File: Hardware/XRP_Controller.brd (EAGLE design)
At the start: 63.5 x 54 mm, 219 parts, among them J1 POWER_JACKPOWER_JACK_SLOT, J12 Vertical Qwiic Connector, J13 Vertical Qwiic Connector, J14 Vertical Qwiic Connector, J3 JST_6_PIN_VERTICAL, J4 JST_6_PIN_VERTICAL, J5 JST_6_PIN_VERTICAL, J6 JST_6_PIN_VERTICAL, J9 Vertical Qwiic Connector, Q3 20V/4.2A/52mΩ/1.4W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

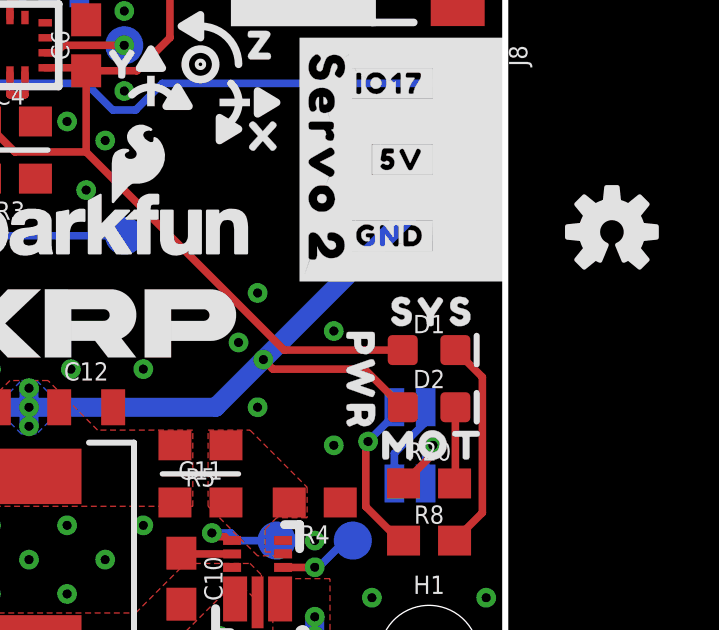
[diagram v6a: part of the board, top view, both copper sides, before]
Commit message: Put OSHW logo back onto board
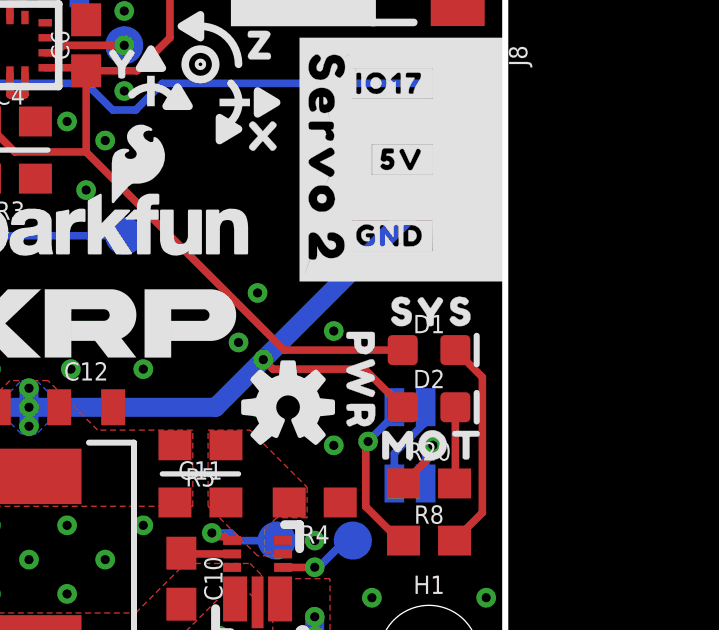
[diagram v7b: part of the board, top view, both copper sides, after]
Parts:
- moved LOGO1 12.3 mm to (56.3, 10.8)
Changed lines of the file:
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@@
 <element name="FD3" library="SparkFun-Aesthetics" package="FIDUCIAL-1X2" value="FIDUCIAL1X2" x="2.54" y="5.08" smashed="yes"/>
 <element name="FD4" library="SparkFun-Aesthetics" package="FIDUCIAL-1X2" value="FIDUCIAL1X2" x="2.54" y="5.08" smashed="yes" rot="MR0"/>
-<element name="LOGO1" library="SparkFun-Aesthetics" package="OSHW-LOGO-S" value="OSHW-LOGOS" x="67.056" y="16.637" smashed="yes"/>
+<element name="LOGO1" library="SparkFun-Aesthetics" package="OSHW-LOGO-S" value="OSHW-LOGOS" x="56.261" y="10.795" smashed="yes"/>
 <element name="LOGO3" library="SparkFun-Aesthetics" package="SFE_LOGO_NAME_FLAME_.3" value="SFE_LOGO_NAME_FLAME.3_INCH" x="37.465" y="41.91" smashed="yes" rot="MR0"/>
 <element name="H1" library="SparkFun-Hardware" package="STAND-OFF" value="STAND-OFF" x="60.96" y="2.54" smashed="yes">

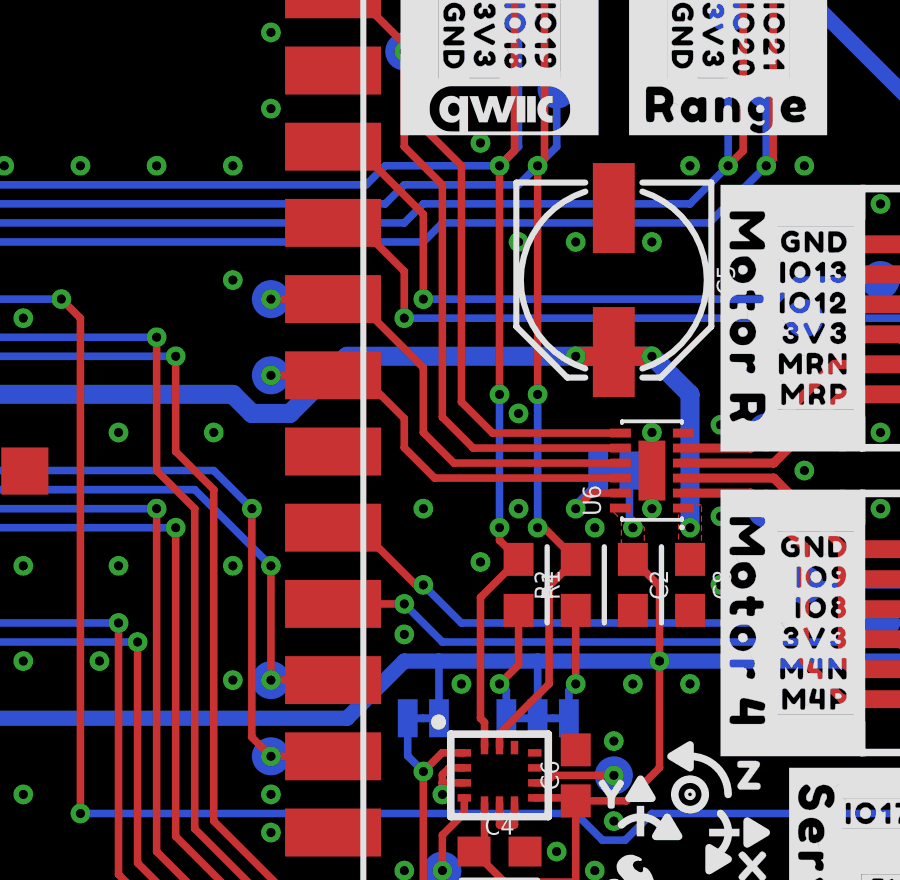
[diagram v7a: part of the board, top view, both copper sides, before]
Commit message: Add OpenSTEM logos
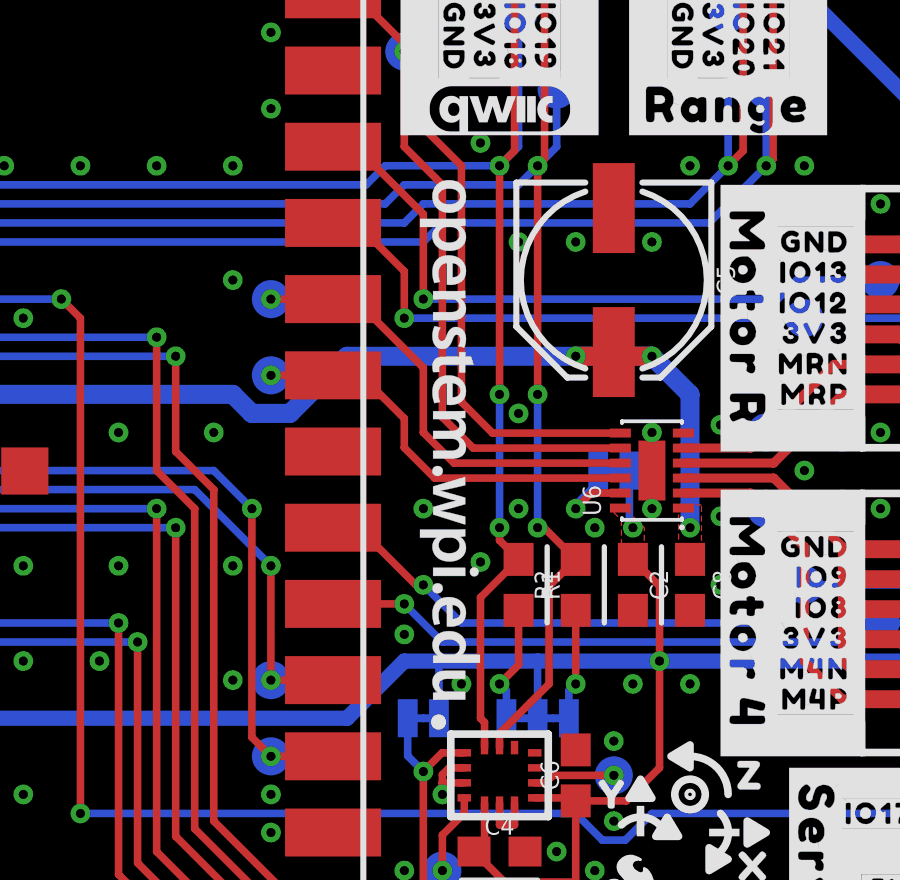
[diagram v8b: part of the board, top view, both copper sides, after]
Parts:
- added U$72: (no value), XRP_COMPONENTS:OPENSTEM_LOGO
- added U$94: (no value), XRP_COMPONENTS:OPENSTEM_URL_SMALL
- added U$97: (no value), XRP_COMPONENTS:OPENSTEM_URL_LARGE
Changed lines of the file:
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@@
 <element name="U$96" library="output" package="#SYS#0" value="" x="59.436" y="10.795" smashed="yes" rot="MR0"/>
 <element name="U$73" library="output" package="#PWR#0" value="" x="62.23" y="9.525" smashed="yes" rot="MR90"/>
+<element name="U$72" library="XRP_COMPONENTS" package="OPENSTEM_LOGO" value="" x="27.305" y="24.511" smashed="yes" rot="MR0"/>
+<element name="U$94" library="XRP_COMPONENTS" package="OPENSTEM_URL_SMALL" value="" x="45.339" y="34.036" smashed="yes" rot="R270"/>
+<element name="U$97" library="XRP_COMPONENTS" package="OPENSTEM_URL_LARGE" value="" x="27.305" y="16.891" smashed="yes" rot="MR0"/>
 </elements>
 <signals>
